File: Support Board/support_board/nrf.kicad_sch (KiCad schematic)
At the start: 27 parts, among them U1 ${ALTIUM_VALUE}, U2 ${ALTIUM_VALUE}, Y1 32 MHz, Y2 32.768 kHz

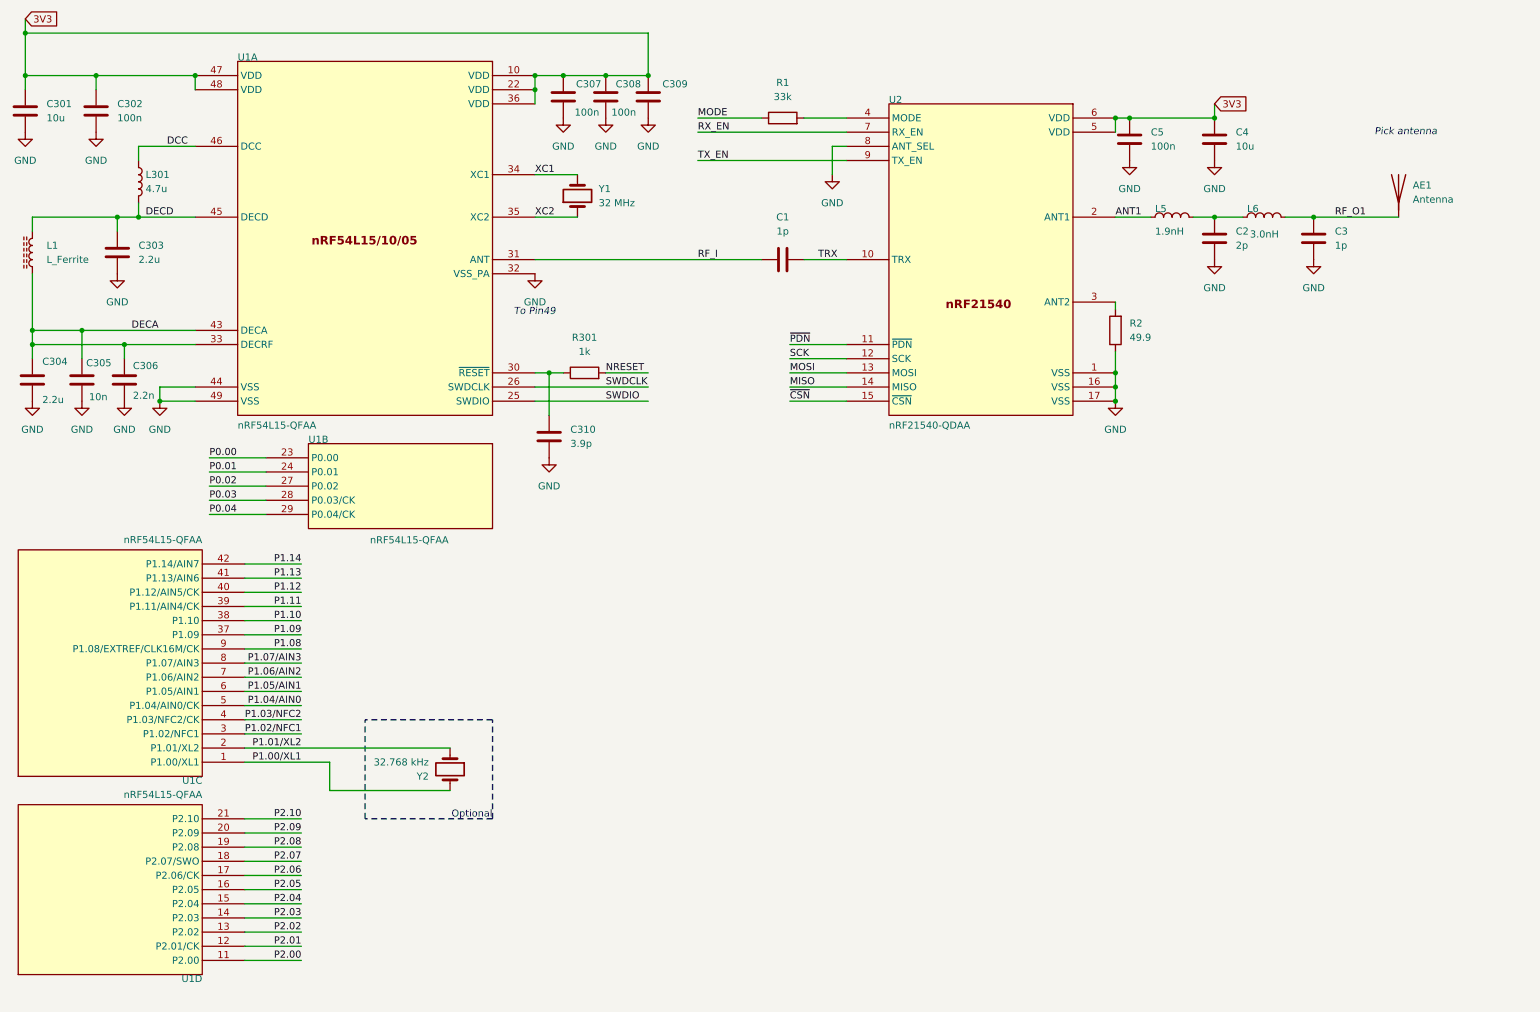
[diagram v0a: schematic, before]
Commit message: Updated PM files and Schematics in the Support Board
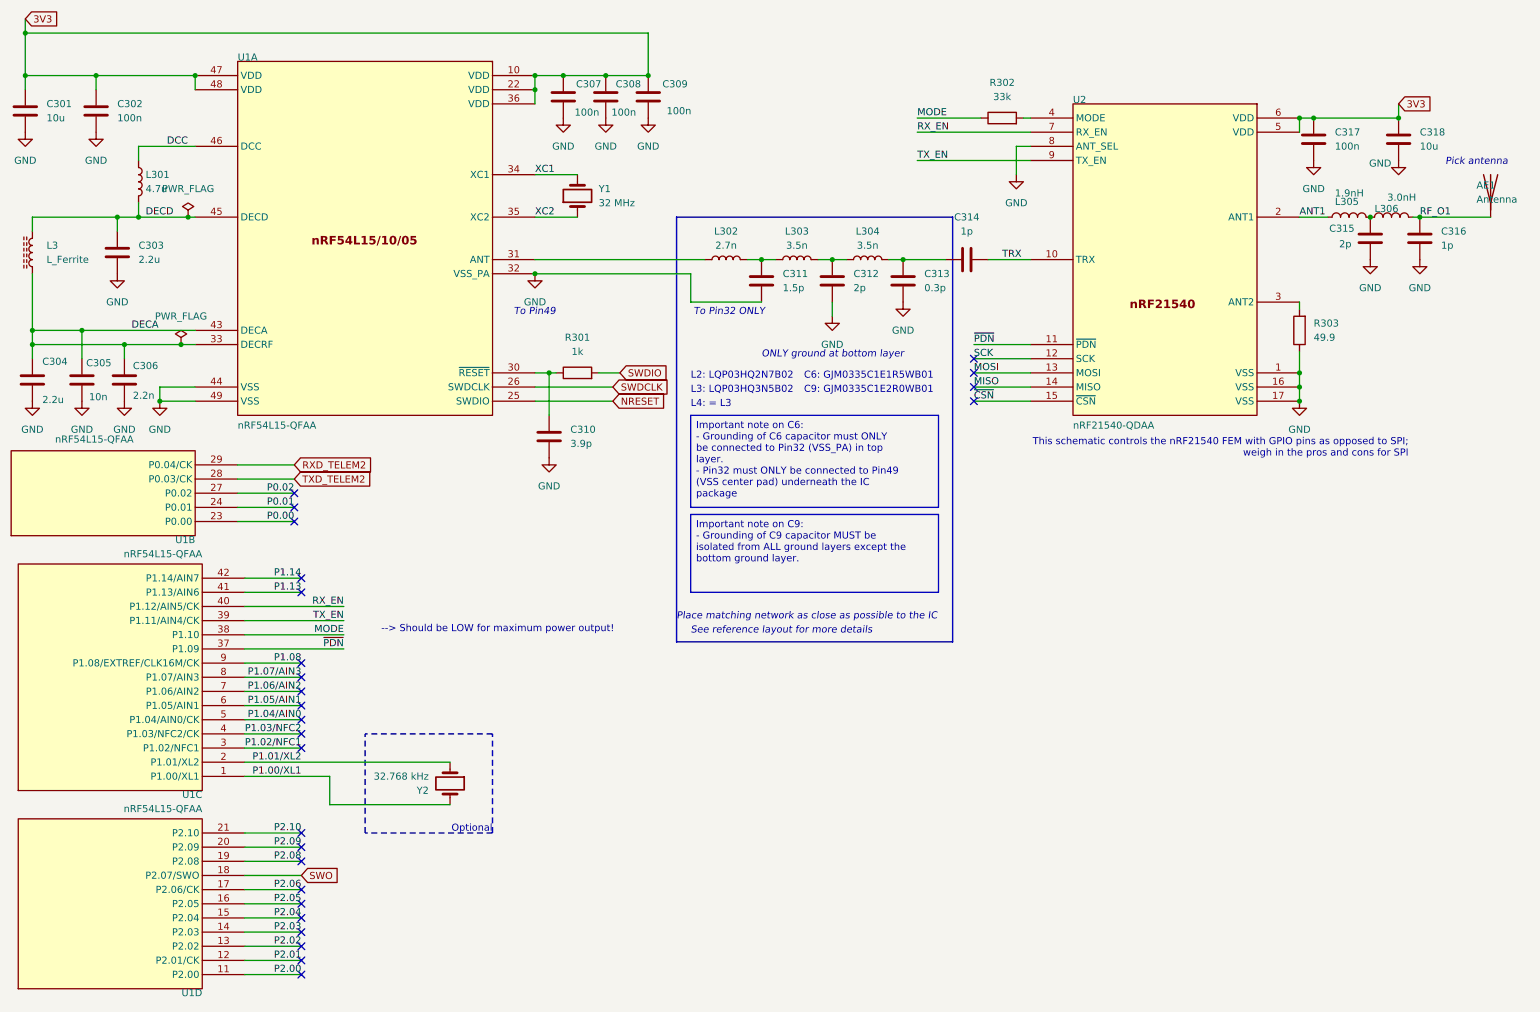
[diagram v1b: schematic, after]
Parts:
- added C311: 1.5p, Capacitor_SMD:C_0402_1005Metric, symbol Device:C
- added C312: 2p, Capacitor_SMD:C_0402_1005Metric, symbol Device:C
- added C313: 0.3p, Capacitor_SMD:C_0402_1005Metric, symbol Device:C
- added L302: 2.7n, Inductor_SMD:L_0402_1005Metric, symbol Device:L
- added L303, L304: 3.5n, Inductor_SMD:L_0402_1005Metric, symbol Device:L
- AE1: footprint (none) -> RF_Antenna:Texas_SWRA117D_2.4GHz_Right
- C301: footprint (none) -> Capacitor_SMD:C_0603_1608Metric
- C302, C303, C304, C305, C306, C307, C308, C309, C310: footprint (none) -> Capacitor_SMD:C_0402_1005Metric
- C314: renamed from C1; footprint (none) -> Capacitor_SMD:C_0402_1005Metric
- C315: renamed from C2; footprint (none) -> Capacitor_SMD:C_0402_1005Metric
- C316: renamed from C3; footprint (none) -> Capacitor_SMD:C_0402_1005Metric
- C317: renamed from C5; footprint (none) -> Capacitor_SMD:C_0402_1005Metric
- C318: renamed from C4; footprint (none) -> Capacitor_SMD:C_0603_1608Metric
- L3: renamed from L1; footprint (none) -> Inductor_SMD:L_0201_0603Metric_Pad0.64x0.40mm_HandSolder
- L301: footprint (none) -> Inductor_SMD:L_0402_1005Metric
- L305: renamed from L5; footprint INDC0603X03L_C -> Inductor_SMD:L_0402_1005Metric
- L306: renamed from L6; footprint INDC0603X03L_C -> Inductor_SMD:L_0402_1005Metric
- R302: renamed from R1; footprint (none) -> Resistor_SMD:R_0402_1005Metric
- R303: renamed from R2; footprint (none) -> Resistor_SMD:R_0402_1005Metric
- U2: footprint QFN65P400X400X65_HS-17N -> Package_DFN_QFN:QFN-16-1EP_1.8x2.6mm_P0.4mm_EP0.7x1.5mm
- Y1, Y2: footprint (none) -> Crystal:Crystal_SMD_HC49-SD
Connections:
- net P1.09 is gone; now on net ~{PDN}: U1.37 (P1.09)
- net P1.10 is gone; now on net MODE: U1.38 (P1.10)
- net P1.11 is gone; now on net TX_EN: U1.39 (P1.11/AIN4/CK)
- net P1.12 is gone; now on net RX_EN: U1.40 (P1.12/AIN5/CK)
- net GND: now also C311.2, C312.2, C313.2
- net NRESET: now also U1.25 (SWDIO); no longer R301.2
- net SWDIO: now also R301.2; no longer U1.25 (SWDIO)
- net P0.03 renamed TXD_TELEM2
- net P0.04 renamed RXD_TELEM2
- net P2.07 renamed SWO
- net RF_I: no longer names the net of C314.1
- net RF_I: now also C313.1, L304.2; no longer U1.31 (ANT)
- new net: C311.1, L302.2, L303.1
- new net: C312.1, L303.2, L304.1
- new net: L302.1, U1.31 (ANT)
- no-connect marks 0 -> 26
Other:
- note added: "--> Should be LOW for maximum power output!"
- note added: "C6: GJM0335C1E1R5WB01"
- note added: "C9: GJM0335C1E2R0WB01"
- note added: "L2: LQP03HQ2N7B02"
- note added: "L3: LQP03HQ3N5B02"
- note added: "L4: = L3"
- note added: "ONLY ground at bottom layer"
- note added: "Place matching network as close as possible to the IC"
- note added: "See reference layout for more details"
- note added: "This schematic controls the nRF21540 FEM with GPIO pins as opposed to SPI; weigh in the pros and cons for SPI"
- note added: "To Pin32 ONLY"
- moved on the sheet: AE1, C314, C315, C316, C317, C318, L305, L306, R301, R302, R303, U1B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
